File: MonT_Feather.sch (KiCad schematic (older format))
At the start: 11 parts, among them J1 Adafruit_Feather, J2 DB25_Male, U1 MAX3232

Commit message: DSR_TTL pulldown
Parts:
- added R1: 15k, 0_LOCAL:R_0805, symbol 0_LOCAL:R_Small_US
- JP1: footprint 0_LOCAL:JP -> 0_LOCAL:JP_H
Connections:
- wire segments 44 -> 45
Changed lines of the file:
@@
 $EndComp
 Wire Wire Line
-	7200 4500 6300 4500
-Wire Wire Line
-	7200 4970 8210 4970
-Wire Wire Line
-	7200 4500 7200 4970
-Wire Wire Line
-	8210 4770 7400 4770
-Wire Wire Line
-	7400 4770 7400 4100
-Wire Wire Line
-	7400 4100 6300 4100
-Wire Wire Line
-	4700 4500 4000 4500
-Wire Wire Line
-	4000 4500 4000 3860
-Wire Wire Line
-	4000 3860 3150 3860
-Wire Wire Line
-	4700 4100 4200 4100
-Wire Wire Line
-	4200 4100 4200 3960
-Wire Wire Line
-	4200 3960 3150 3960
+	6700 4500 6300 4500
+Wire Wire Line
+	6700 4970 8210 4970
+Wire Wire Line
+	6700 4500 6700 4970
+Wire Wire Line
+	8210 4770 6900 4770
+Wire Wire Line
+	6900 4770 6900 4100
+Wire Wire Line
+	6900 4100 6300 4100
+Wire Wire Line
+	4700 4500 4200 4500
+Wire Wire Line
+	4200 4500 4200 3860
+Wire Wire Line
+	4200 3860 3150 3860
+Wire Wire Line
+	4700 4100 3800 4100
+Wire Wire Line
+	3800 4100 3800 3960
+Wire Wire Line
+	3800 3960 3150 3960
 $Comp
 L 0_LOCAL:GND #PWR04
@@
 F 0 "JP1" H 7850 4430 50  0000 C CNN
 F 1 "Jumper_2_Bridged" H 8000 4480 50  0001 C CNN
-F 2 "0_LOCAL:JP" H 7970 4370 50  0001 C CNN
+F 2 "0_LOCAL:JP_H" H 7970 4370 50  0001 C CNN
 F 3 "~" H 7970 4370 50  0001 C CNN
 	1    7970 4370
@@
 	7770 4570 7770 4370
 $Comp
-L power:+3V3 #PWR0106
+L 0_LOCAL:+3V3 #PWR0106
 U 1 1 5F3FB811
 P 2050 3460
@@
 $EndComp
 $Comp
-L power:+3V3 #PWR0107
+L 0_LOCAL:+3V3 #PWR0107
 U 1 1 5F400D96
 P 5500 2600
@@
 	5500 2700 5500 2600
 Wire Wire Line
-	6300 4300 7200 4300
-Wire Wire Line
-	7200 4300 7200 4170
+	6300 4300 7400 4300
+Wire Wire Line
+	7400 4300 7400 4170
 Wire Wire Line
 	7600 3870 7600 4700
@@
 DSR
 Wire Wire Line
-	3150 4360 4200 4360
-Wire Wire Line
-	4200 4360 4200 4300
-Wire Wire Line
-	4200 4300 4700 4300
+	3150 4360 3800 4360
+Wire Wire Line
+	3800 4360 3800 4300
+Wire Wire Line
+	3800 4300 4700 4300
 Text Label 3150 4360 0    50   ~ 0
 DTR_TTL
@@
 	3800 4700 3800 4460
 Wire Wire Line
-	3800 4460 3150 4460
+	3800 4460 3380 4460
 Text Label 3150 4460 0    50   ~ 0
 DSR_TTL
@@
 DSR_TTL
 Wire Wire Line
-	7200 4170 7770 4170
+	7400 4170 7770 4170
 Wire Wire Line
 	7600 3870 8210 3870
@@
 Wire Wire Line
 	7770 4120 7770 4170
+$Comp
+L 0_LOCAL:R_Small_US R1
+U 1 1 5F3E0320
+P 3380 4560
+F 0 "R1" H 3450 4620 50  0000 L CNN
+F 1 "15k" H 3450 4520 50  0000 L CNN
+F 2 "0_LOCAL:R_0805" H 3380 4560 50  0001 C CNN
+F 3 "~" H 3380 4560 50  0001 C CNN
+	1    3380 4560
+	1    0    0    -1
+$EndComp
+Connection ~ 3380 4460
+Wire Wire Line
+	3380 4460 3150 4460
+$Comp
+L 0_LOCAL:GND #PWR0108
+U 1 1 5F3E0D9B
+P 3380 4660
+F 0 "#PWR0108" H 3380 4410 50  0001 C CNN
+F 1 "GND" H 3400 4470 50  0000 C CNN
+F 2 "" H 3380 4660 50  0001 C CNN
+F 3 "" H 3380 4660 50  0001 C CNN
+	1    3380 4660
+	1    0    0    -1
+$EndComp
 $EndSCHEMATC

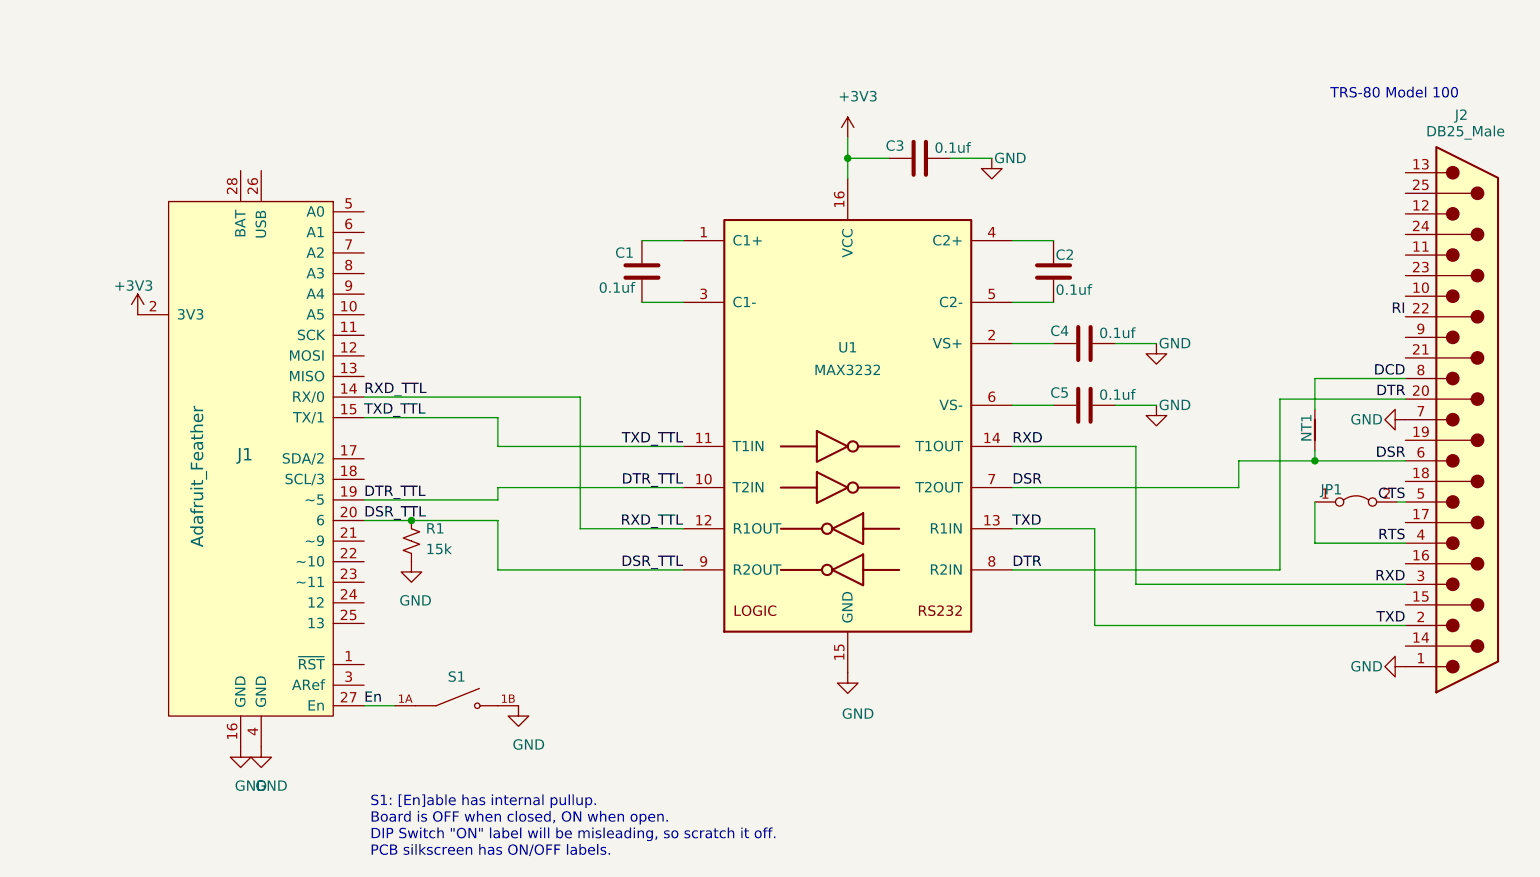
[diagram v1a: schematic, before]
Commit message: boms and remove dsr pulldown
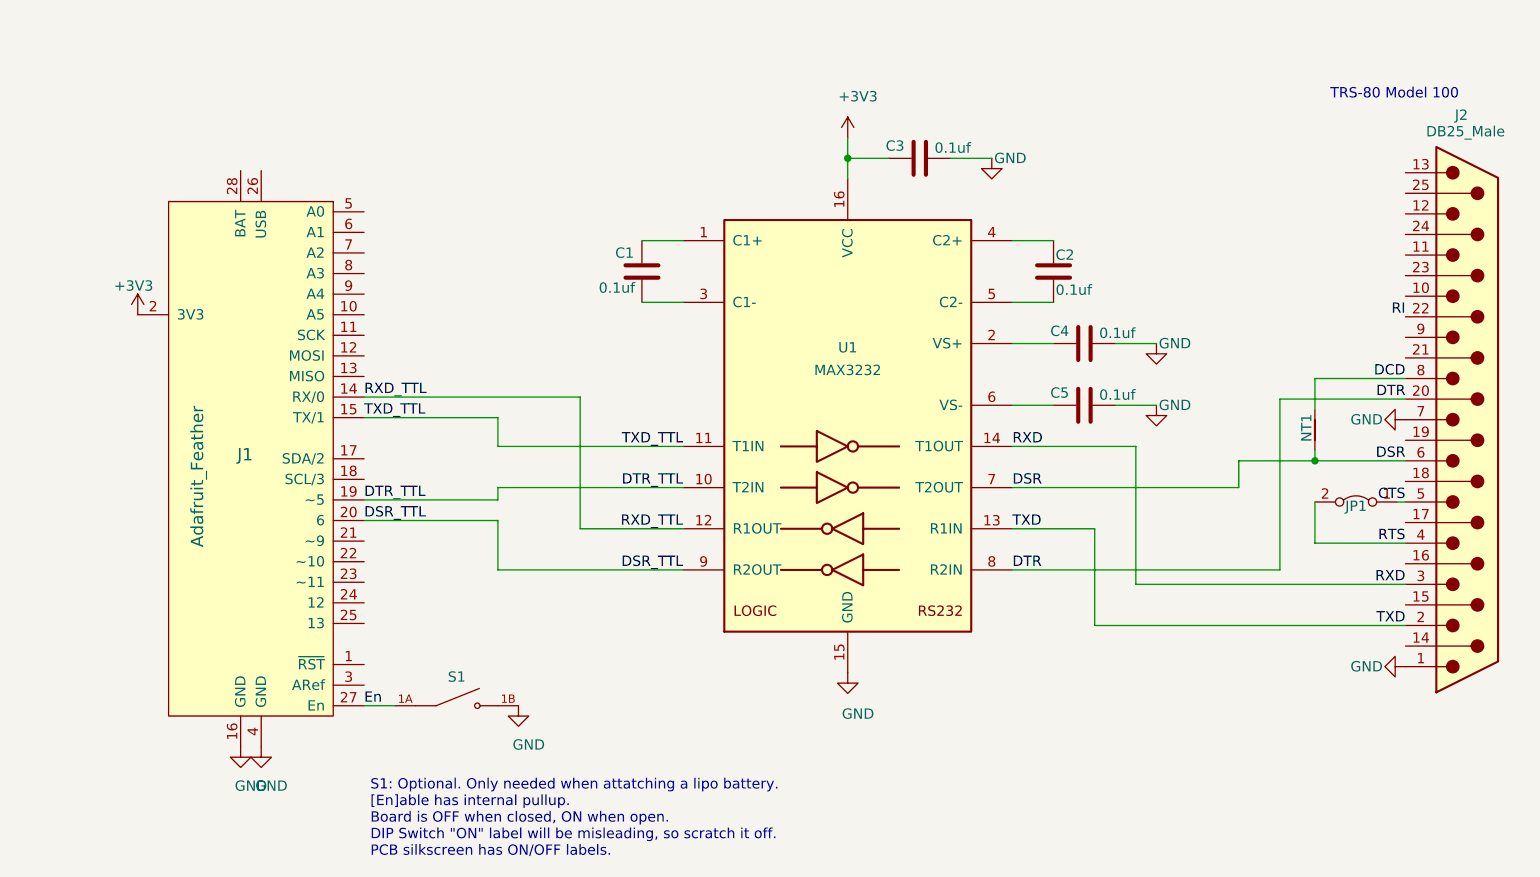
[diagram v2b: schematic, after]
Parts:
- removed R1: 15k, 0_LOCAL:R_0805, symbol 0_LOCAL:R_Small_US
- JP1: footprint 0_LOCAL:JP_H -> 0_LOCAL:PinHeader_1x02_P2.54mm_Horizontal
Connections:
- net CTS: now also JP1.1 (A); no longer JP1.2 (B)
- net RTS: now also JP1.2 (B); no longer JP1.1 (A)
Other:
- note added: "S1: Optional. Only needed when attatching a lipo battery.\n[En]able has internal pullup.\nBoard is OFF when closed, ON when open.\nDIP Switch "ON" label will be misleading, so scratch it off.\nPCB silkscreen has ON/OFF labels."
- note removed: "S1: [En]able has internal pullup.\nBoard is OFF when closed, ON when open.\nDIP Switch "ON" label will be misleading, so scratch it off.\nPCB silkscreen has ON/OFF labels."
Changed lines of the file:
@@
 $EndComp
 Text Notes 3180 6100 0    50   ~ 0
-S1: [En]able has internal pullup.\nBoard is OFF when closed, ON when open.\nDIP Switch "ON" label will be misleading, so scratch it off.\nPCB silkscreen has ON/OFF labels.
+S1: Optional. Only needed when attatching a lipo battery.\n[En]able has internal pullup.\nBoard is OFF when closed, ON when open.\nDIP Switch "ON" label will be misleading, so scratch it off.\nPCB silkscreen has ON/OFF labels.
 $Comp
 L 0_LOCAL:Jumper_2_Bridged JP1
 U 1 1 5F3DBD1F
 P 7970 4370
-F 0 "JP1" H 7850 4430 50  0000 C CNN
+F 0 "JP1" H 7970 4350 50  0000 C CNN
 F 1 "Jumper_2_Bridged" H 8000 4480 50  0001 C CNN
-F 2 "0_LOCAL:JP_H" H 7970 4370 50  0001 C CNN
+F 2 "0_LOCAL:PinHeader_1x02_P2.54mm_Horizontal" H 7970 4370 50  0001 C CNN
 F 3 "~" H 7970 4370 50  0001 C CNN
 	1    7970 4370
-	1    0    0    -1
+	-1   0    0    -1
 $EndComp
 Wire Wire Line
@@
 Wire Wire Line
 	3800 4700 3800 4460
-Wire Wire Line
-	3800 4460 3380 4460
 Text Label 3150 4460 0    50   ~ 0
 DSR_TTL
@@
 Wire Wire Line
 	7770 4120 7770 4170
-$Comp
-L 0_LOCAL:R_Small_US R1
-U 1 1 5F3E0320
-P 3380 4560
-F 0 "R1" H 3450 4620 50  0000 L CNN
-F 1 "15k" H 3450 4520 50  0000 L CNN
-F 2 "0_LOCAL:R_0805" H 3380 4560 50  0001 C CNN
-F 3 "~" H 3380 4560 50  0001 C CNN
-	1    3380 4560
-	1    0    0    -1
-$EndComp
-Connection ~ 3380 4460
 Wire Wire Line
-	3380 4460 3150 4460
-$Comp
-L 0_LOCAL:GND #PWR0108
-U 1 1 5F3E0D9B
-P 3380 4660
-F 0 "#PWR0108" H 3380 4410 50  0001 C CNN
-F 1 "GND" H 3400 4470 50  0000 C CNN
-F 2 "" H 3380 4660 50  0001 C CNN
-F 3 "" H 3380 4660 50  0001 C CNN
-	1    3380 4660
-	1    0    0    -1
-$EndComp
+	3150 4460 3800 4460
 $EndSCHEMATC
